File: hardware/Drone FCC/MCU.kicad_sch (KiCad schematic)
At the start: 1 part

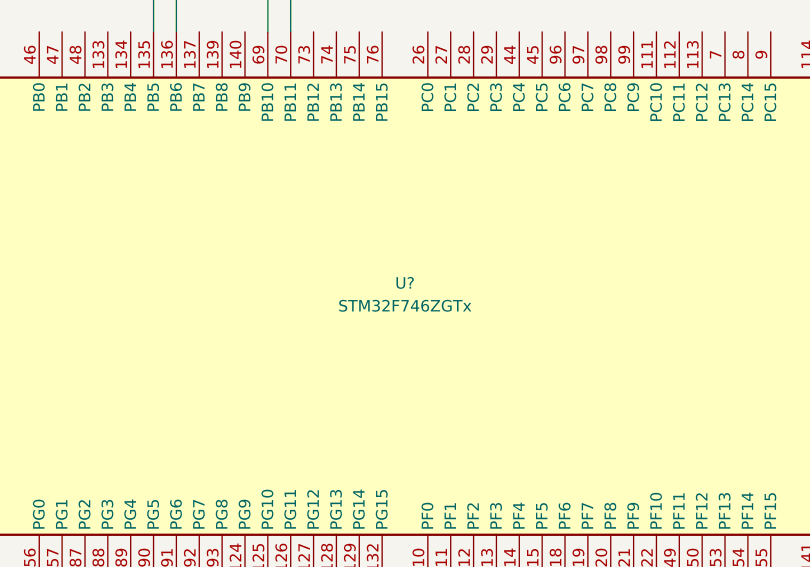
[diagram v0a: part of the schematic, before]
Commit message: changed mag connector for GPS module DF-13
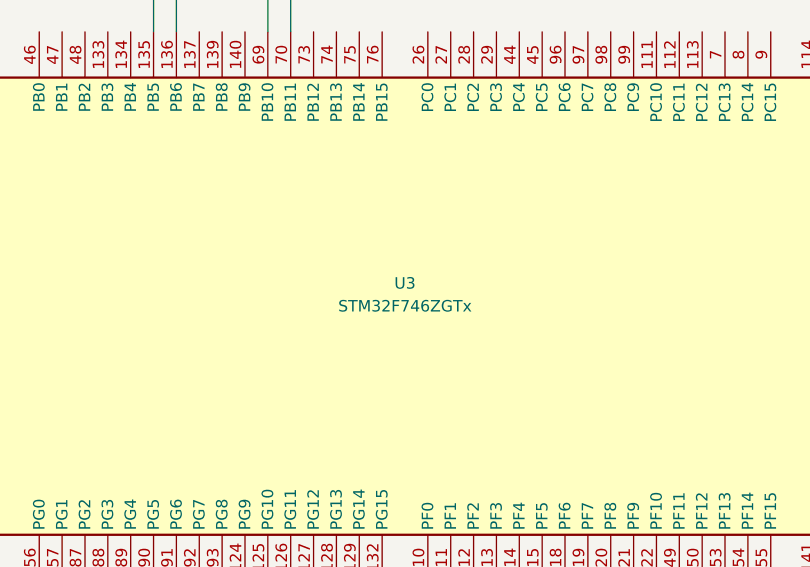
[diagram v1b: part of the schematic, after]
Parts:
- gave numbers to parts that had none: 1
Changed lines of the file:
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@@
   (symbol (lib_id "MCU_ST_STM32F7:STM32F746ZGTx") (at 146.685 78.105 90) (unit 1)
     (in_bom yes) (on_board yes)
-    (property "Reference" "U?" (id 0) (at 146.685 75.565 90))
+    (property "Reference" "U3" (id 0) (at 146.685 75.565 90))
     (property "Value" "STM32F746ZGTx" (id 1) (at 146.685 78.105 90))
     (property "Footprint" "Package_QFP:LQFP-144_20x20mm_P0.5mm" (id 2) (at 233.045 103.505 0)

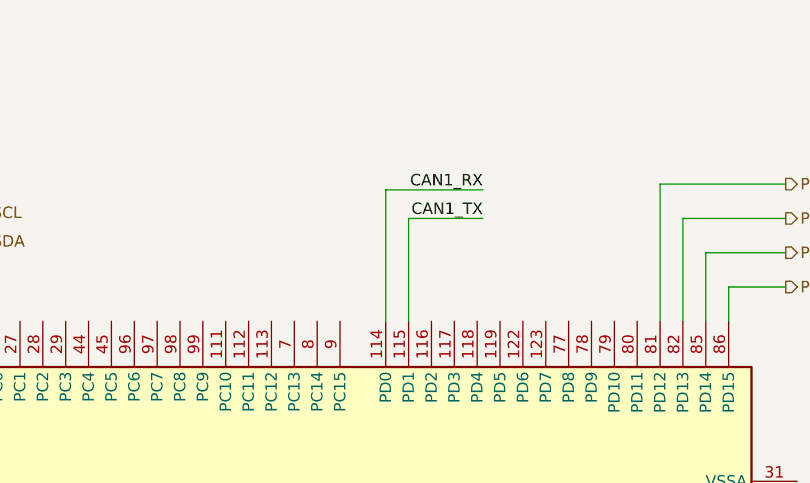
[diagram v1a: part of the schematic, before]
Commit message: add functional schematic for microSD
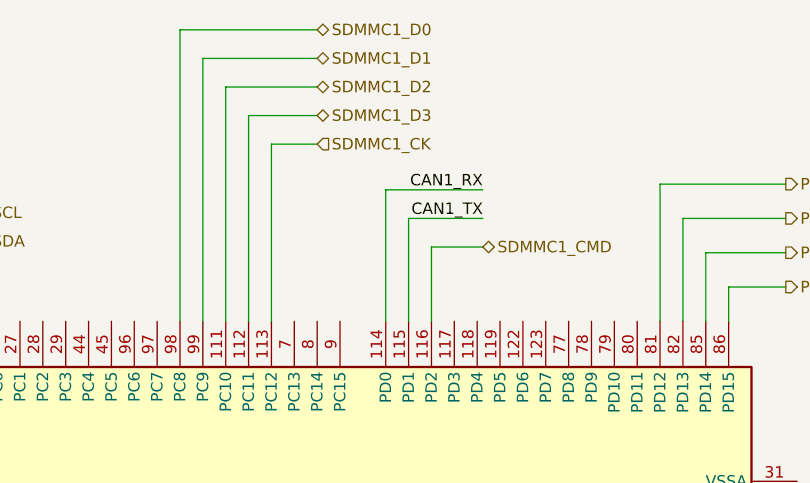
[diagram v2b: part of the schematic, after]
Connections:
- net SDMMC1_D2: now reaches U3.111 (PC10)
- net SDMMC1_D3: now reaches U3.112 (PC11)
- net SDMMC1_CK: now reaches U3.113 (PC12)
- net SDMMC1_CMD: now reaches U3.116 (PD2)
- net SDMMC1_D0: now reaches U3.98 (PC8)
- net SDMMC1_D1: now reaches U3.99 (PC9)
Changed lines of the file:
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@@
+    (stroke (width 0) (type default) (color 0 0 0 0))
+  )
+  (wire (pts (xy 179.705 27.94) (xy 184.785 27.94))
+    (stroke (width 0) (type default) (color 0 0 0 0))
+  )
+  (wire (pts (xy 179.705 27.94) (xy 179.705 47.625))
+    (stroke (width 0) (type default) (color 0 0 0 0))
+  )
+  (wire (pts (xy 174.625 21.59) (xy 184.785 21.59))
     (stroke (width 0) (type default) (color 0 0 0 0))
   )
@@
     (stroke (width 0) (type default) (color 0 0 0 0))
   )
+  (wire (pts (xy 172.085 18.415) (xy 184.785 18.415))
+    (stroke (width 0) (type default) (color 0 0 0 0))
+  )
   (wire (pts (xy 80.645 28.575) (xy 80.645 47.625))
     (stroke (width 0) (type default) (color 0 0 0 0))
@@
     (stroke (width 0) (type default) (color 0 0 0 0))
   )
+  (wire (pts (xy 169.545 15.24) (xy 169.545 47.625))
+    (stroke (width 0) (type default) (color 0 0 0 0))
+  )
   (wire (pts (xy 85.725 47.625) (xy 85.725 31.115))
     (stroke (width 0) (type default) (color 0 0 0 0))
@@
     (stroke (width 0) (type default) (color 0 0 0 0))
   )
+  (wire (pts (xy 174.625 21.59) (xy 174.625 47.625))
+    (stroke (width 0) (type default) (color 0 0 0 0))
+  )
   (wire (pts (xy 78.105 31.115) (xy 78.105 47.625))
     (stroke (width 0) (type default) (color 0 0 0 0))
@@
     (stroke (width 0) (type default) (color 0 0 0 0))
   )
+  (wire (pts (xy 172.085 18.415) (xy 172.085 47.625))
+    (stroke (width 0) (type default) (color 0 0 0 0))
+  )
+  (wire (pts (xy 177.165 24.765) (xy 184.785 24.765))
+    (stroke (width 0) (type default) (color 0 0 0 0))
+  )
+  (wire (pts (xy 169.545 15.24) (xy 184.785 15.24))
+    (stroke (width 0) (type default) (color 0 0 0 0))
+  )
   (wire (pts (xy 66.675 28.575) (xy 80.645 28.575))
     (stroke (width 0) (type default) (color 0 0 0 0))
@@
     (stroke (width 0) (type default) (color 0 0 0 0))
   )
+  (wire (pts (xy 197.485 39.37) (xy 203.2 39.37))
+    (stroke (width 0) (type default) (color 0 0 0 0))
+  )
   (wire (pts (xy 66.675 34.29) (xy 75.565 34.29))
     (stroke (width 0) (type default) (color 0 0 0 0))
@@
     (stroke (width 0) (type default) (color 0 0 0 0))
   )
+  (wire (pts (xy 177.165 24.765) (xy 177.165 47.625))
+    (stroke (width 0) (type default) (color 0 0 0 0))
+  )
   (wire (pts (xy 222.885 32.385) (xy 222.885 47.625))
     (stroke (width 0) (type default) (color 0 0 0 0))
@@
     (stroke (width 0) (type default) (color 0 0 0 0))
   )
+  (wire (pts (xy 197.485 47.625) (xy 197.485 39.37))
+    (stroke (width 0) (type default) (color 0 0 0 0))
+  )
   (label "CAN2_RX" (at 130.175 33.02 180)
     (effects (font (size 1.27 1.27)) (justify right bottom))
@@
   (label "CAN1_RX" (at 203.2 33.02 180)
     (effects (font (size 1.27 1.27)) (justify right bottom))
+  )
+  (hierarchical_label "SDMMC1_D0" (shape bidirectional) (at 184.785 15.24 0)
+    (effects (font (size 1.27 1.27)) (justify left))
+  )
+  (hierarchical_label "SDMMC1_D1" (shape bidirectional) (at 184.785 18.415 0)
+    (effects (font (size 1.27 1.27)) (justify left))
   )
   (hierarchical_label "SPI1_SCK" (shape output) (at 66.675 34.29 180)
@@
     (effects (font (size 1.27 1.27)) (justify left))
   )
+  (hierarchical_label "SDMMC1_CMD" (shape bidirectional) (at 203.2 39.37 0)
+    (effects (font (size 1.27 1.27)) (justify left))
+  )
   (hierarchical_label "PWM11" (shape output) (at 234.315 128.905 0)
     (effects (font (size 1.27 1.27)) (justify left))
@@
   )
   (hierarchical_label "I2C2_SDA" (shape bidirectional) (at 142.24 38.735 0)
+    (effects (font (size 1.27 1.27)) (justify left))
+  )
+  (hierarchical_label "SDMMC1_D2" (shape bidirectional) (at 184.785 21.59 0)
+    (effects (font (size 1.27 1.27)) (justify left))
+  )
+  (hierarchical_label "SDMMC1_D3" (shape bidirectional) (at 184.785 24.765 0)
     (effects (font (size 1.27 1.27)) (justify left))
   )
@@
     (effects (font (size 1.27 1.27)) (justify left))
   )
+  (hierarchical_label "SDMMC1_CK" (shape input) (at 184.785 27.94 0)
+    (effects (font (size 1.27 1.27)) (justify left))
+  )

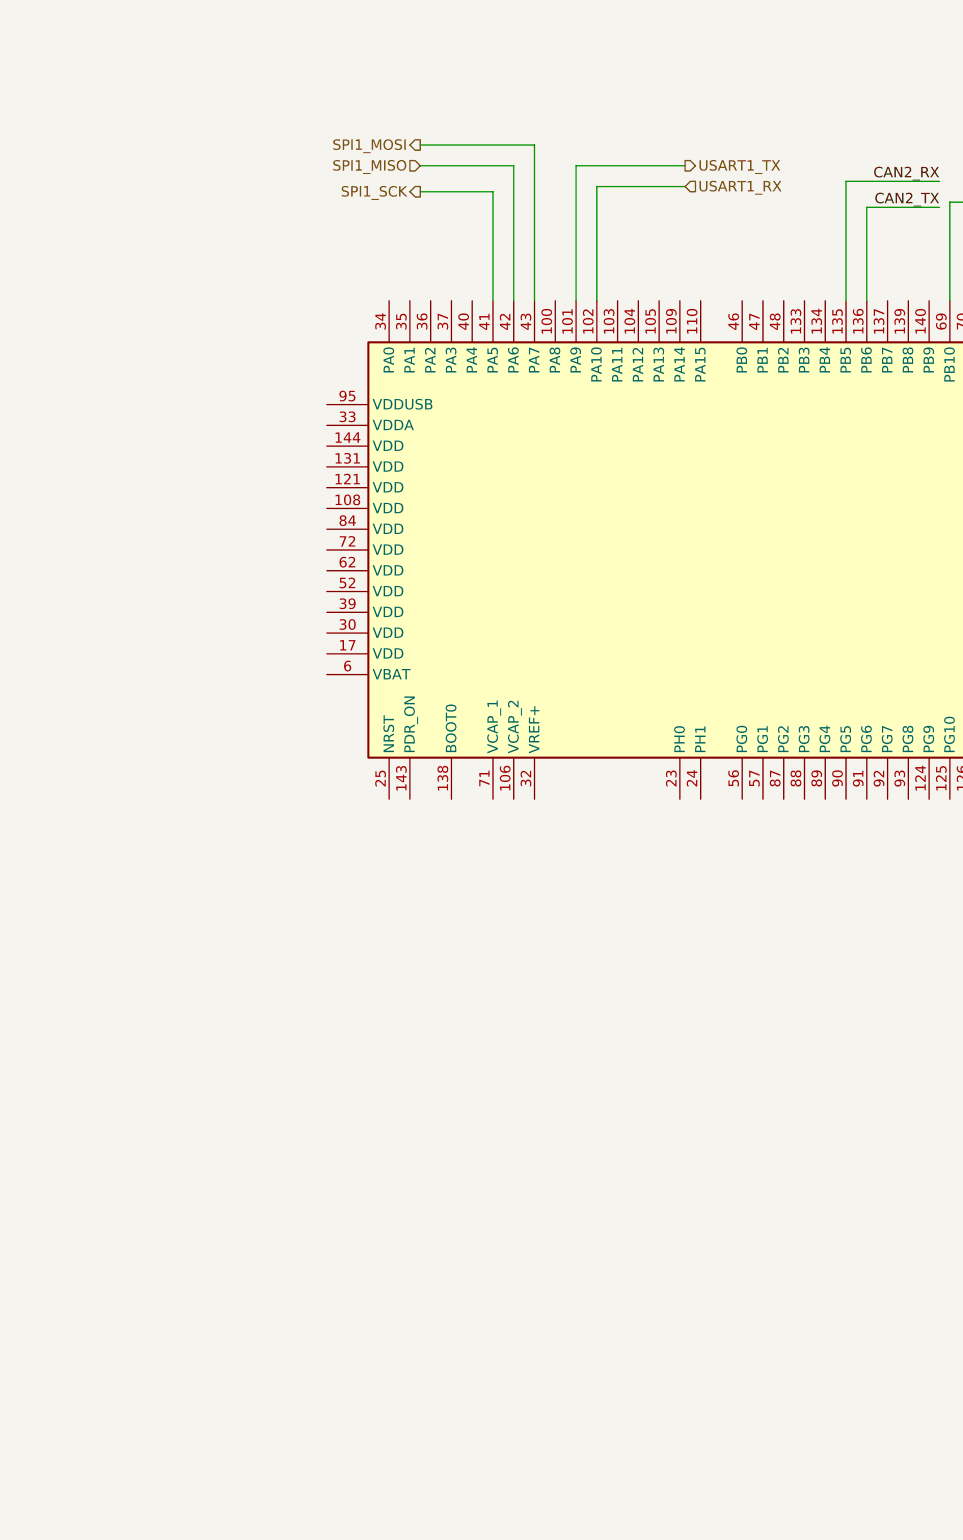
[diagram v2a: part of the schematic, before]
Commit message: add usb TVS diodes and mcu pin assignment
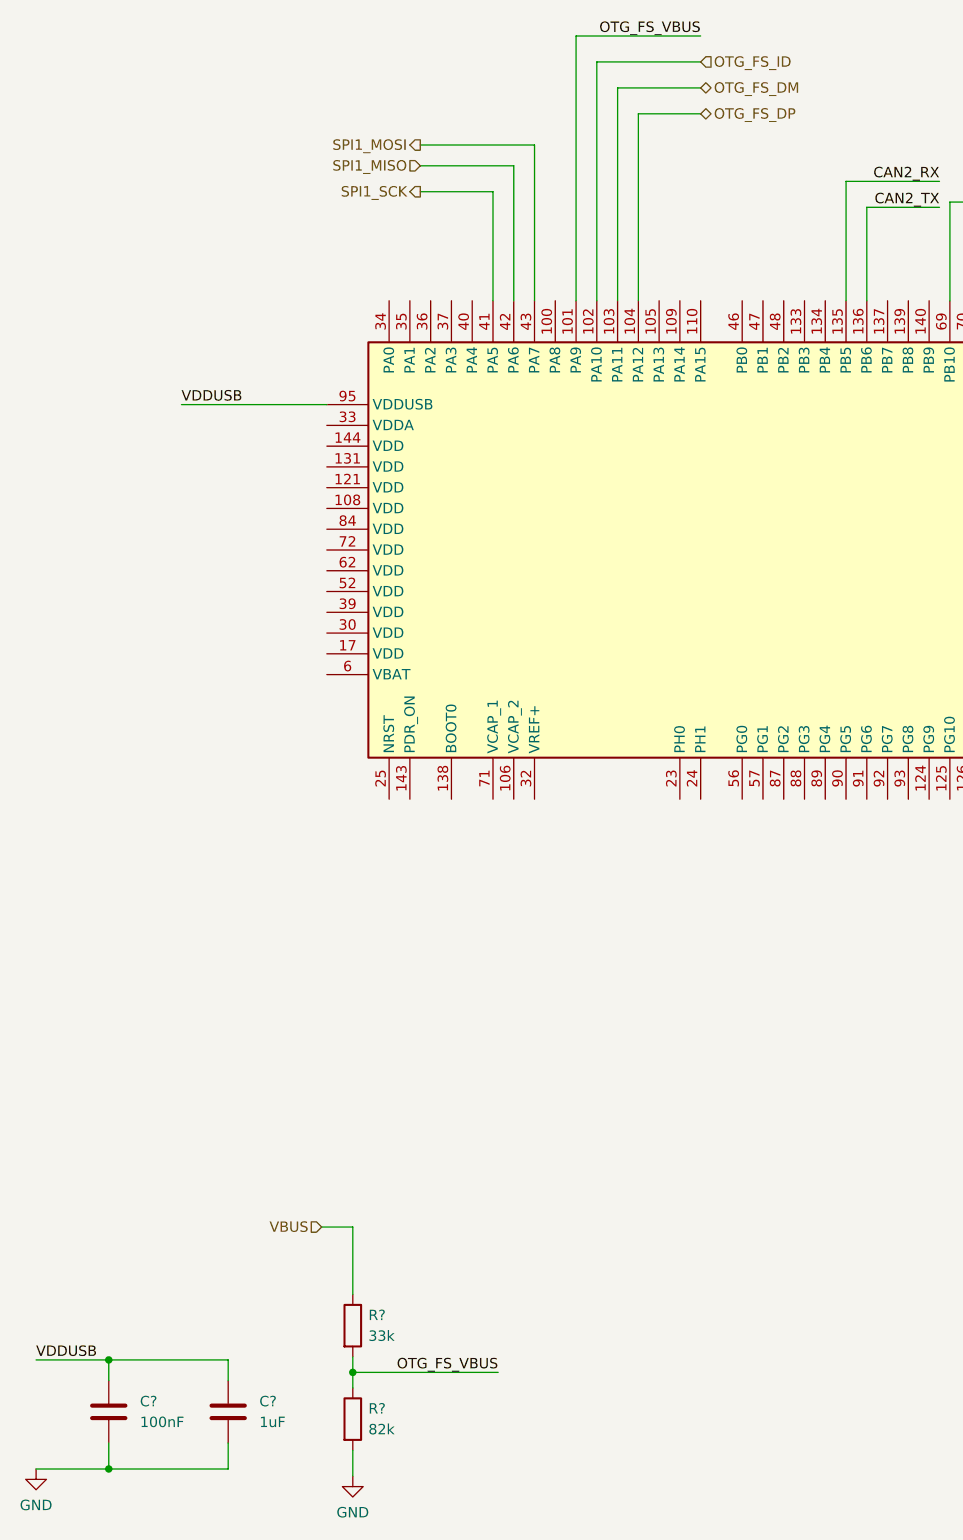
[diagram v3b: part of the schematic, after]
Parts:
- added C?: 100nF, symbol Device:C
- added C?: 1uF, symbol Device:C
- added R?: 82k, symbol Device:R
- added R?: 33k, symbol Device:R
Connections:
- net OTG_FS_DM: now reaches U3.103 (PA11)
- net OTG_FS_DP: now reaches U3.104 (PA12)
- net VDDUSB: now reaches U3.95 (VDDUSB)
- net VDDUSB: now also C?.1, C?.1
- net USART1_RX renamed OTG_FS_ID
- net USART1_TX renamed OTG_FS_VBUS
- net OTG_FS_VBUS: now also R?.1, R?.2
- new net GND: C?.2, C?.2, R?.2
- new net VBUS: R?.1
